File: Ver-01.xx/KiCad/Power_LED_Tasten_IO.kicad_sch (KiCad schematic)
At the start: 45 parts

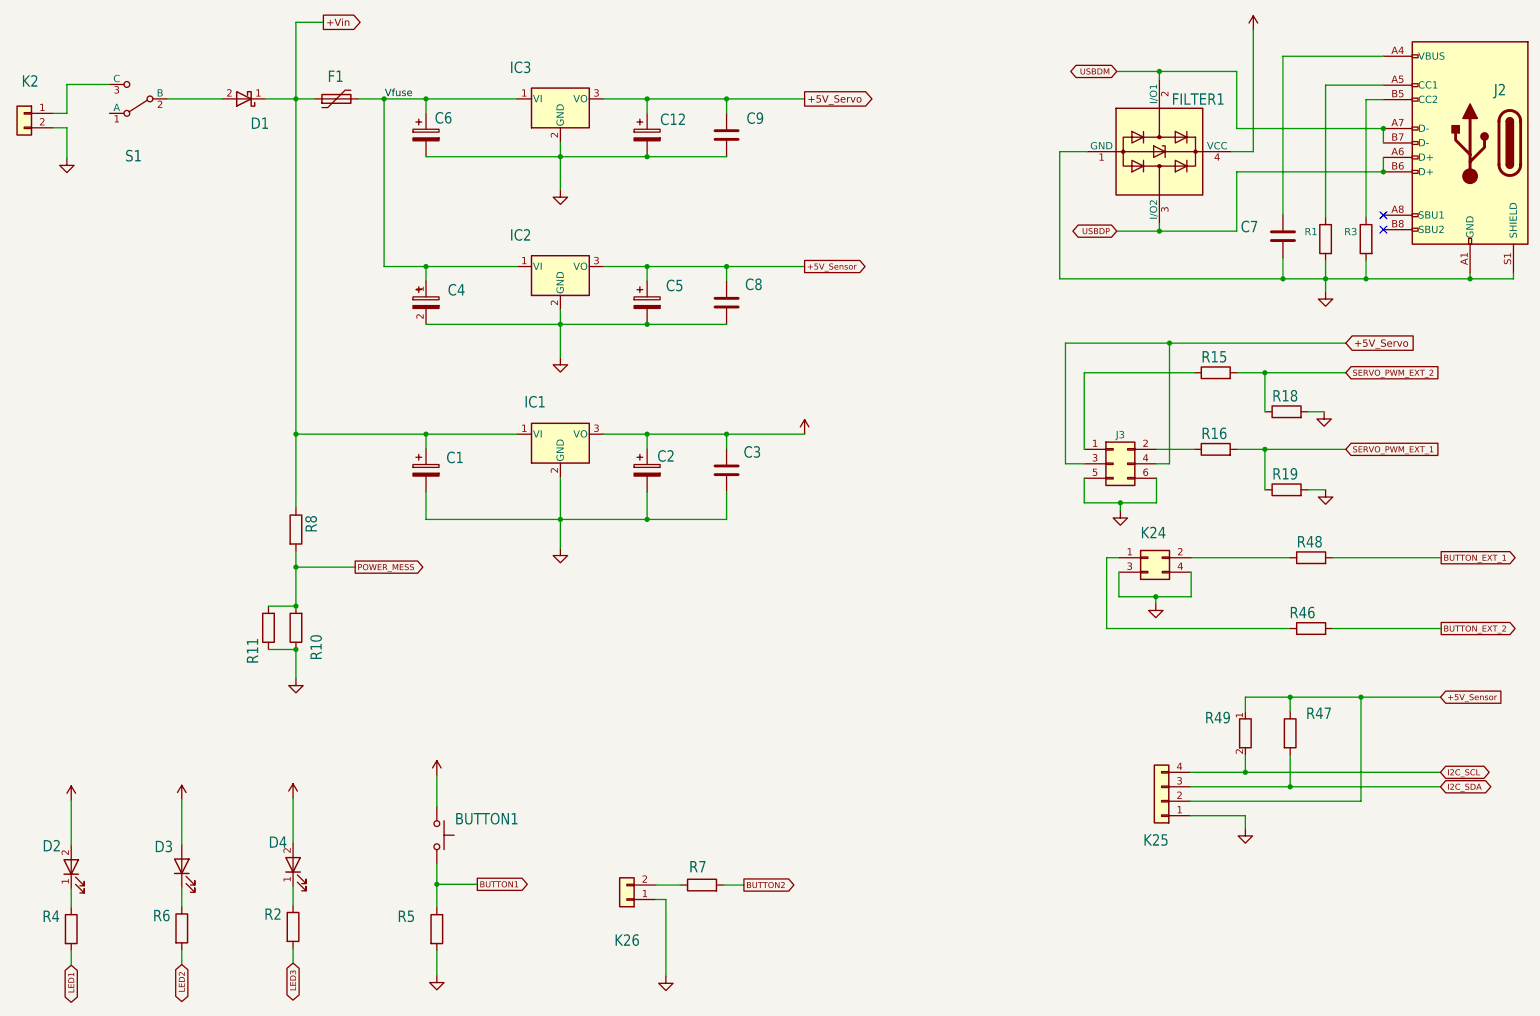
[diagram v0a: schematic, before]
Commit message: Snap to grid
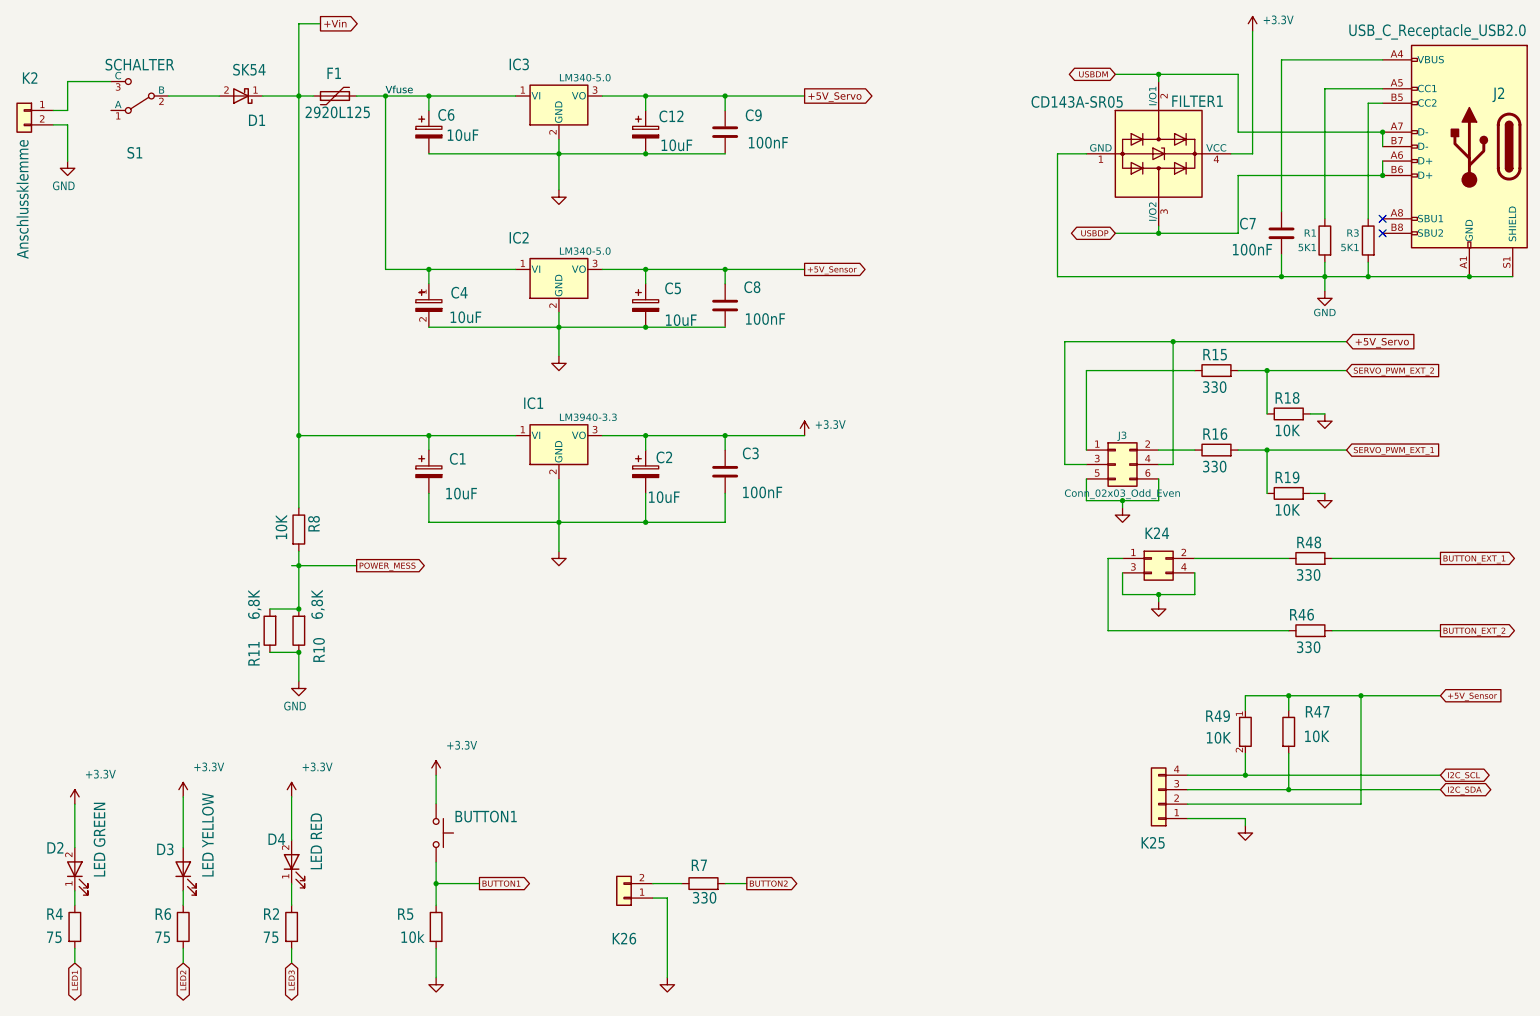
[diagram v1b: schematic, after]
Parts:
- BUTTON1: value (none) -> Taster_SMD; footprint (none) -> Button_Switch_SMD:SW_Push_1P1T_NO_6x6mm_H9.5mm
- C1, C12, C2, C4, C5, C6: value (none) -> 10uF; footprint (none) -> Capacitor_Tantalum_SMD:CP_EIA-3528-12_Kemet-T
- C3, C7, C8, C9: value (none) -> 100nF; footprint (none) -> Capacitor_SMD:C_0805_2012Metric
- D1: value (none) -> SK54; footprint (none) -> Diode_SMD:D_2512_6332Metric
- D2: value (none) -> LED GREEN; footprint (none) -> LED_SMD:LED_0805_2012Metric
- D3: value (none) -> LED YELLOW; footprint (none) -> LED_SMD:LED_0805_2012Metric
- D4: value (none) -> LED RED; footprint (none) -> LED_SMD:LED_0805_2012Metric
- F1: value (none) -> 2920L125; footprint (none) -> Fuse:Fuse_2920_7451Metric
- FILTER1: value (none) -> CD143A-SR05; footprint (none) -> Package_TO_SOT_SMD:SOT-143
- IC1: value (none) -> LM3940-3.3; footprint (none) -> Package_TO_SOT_SMD:SOT-223-3_TabPin2
- IC2, IC3: value (none) -> LM340-5.0; footprint (none) -> Package_TO_SOT_SMD:SOT-223-3_TabPin2
- J2: value (none) -> USB_C_Receptacle_USB2.0; footprint (none) -> Connector_USB:USB_C_Receptacle_JAE_DX07S016JA1R1500
- J3: value (none) -> Conn_02x03_Odd_Even; footprint (none) -> ORB:PinHeader_2x03_P2.54mm_Horizontal
- K2: value (none) -> Anschlussklemme; footprint (none) -> ORB:PinHeader_1x02_P2.54mm_Horizontal
- K24: value (none) -> Stiftleiste_2x02; footprint (none) -> ORB:PinHeader_2x02_P2.54mm_Horizontal
- K25: value (none) -> Stiftleiste_1x04; footprint (none) -> Connector_PinHeader_2.54mm:PinHeader_1x04_P2.54mm_Vertical
- K26: value (none) -> Stiftleiste_1x02_G_2,54; footprint (none) -> Connector_PinHeader_2.54mm:PinHeader_1x02_P2.54mm_Vertical
- R1, R3: value (none) -> 5K1; footprint (none) -> Resistor_SMD:R_0603_1608Metric
- R10, R11: value (none) -> 6,8K; footprint (none) -> Resistor_SMD:R_0603_1608Metric
- R15, R16, R46, R48, R7: value (none) -> 330; footprint (none) -> Resistor_SMD:R_0603_1608Metric
- R18, R19, R47, R49, R8: value (none) -> 10K; footprint (none) -> Resistor_SMD:R_0603_1608Metric
- R2, R4, R6: value (none) -> 75; footprint (none) -> Resistor_SMD:R_0603_1608Metric
- R5: value (none) -> 10k; footprint (none) -> Resistor_SMD:R_0603_1608Metric
- S1: value (none) -> SCHALTER; footprint (none) -> ORB:SW_500SSP1S1M7QEA
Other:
- moved on the sheet: C1, C12, C4, C5, C6, C7, C8, C9, D1, D2, D3, D4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

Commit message: Kleinere Optimierungen
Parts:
- R18, R19, R47, R49, R8: OrderNr YAG1290CT-ND -> YAG1290DKR-ND
- R5: value 10k -> 10K; MPN RC0603FR-10330RL -> RC0603FR-0710KP; OrderNr 13-RC0603FR-10330RLCT-ND -> YAG1290DKR-ND
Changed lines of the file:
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@@
       (effects (font (size 1.27 1.27)) hide)
     )
-    (property "OrderNr" "YAG1290CT-ND" (id 6) (at 238.76 86.36 0)
+    (property "OrderNr" "YAG1290DKR-ND" (id 6) (at 238.76 86.36 0)
       (effects (font (size 1.27 1.27)) hide)
     )
@@
       (effects (font (size 1.27 1.27)) hide)
     )
-    (property "OrderNr" "YAG1290CT-ND" (id 6) (at 238.76 100.33 0)
+    (property "OrderNr" "YAG1290DKR-ND" (id 6) (at 238.76 100.33 0)
       (effects (font (size 1.27 1.27)) hide)
     )
@@
       (effects (font (size 2 1.7)) (justify right bottom))
     )
-    (property "Value" "10k" (id 1) (at 86.868 179.578 0)
+    (property "Value" "10K" (id 1) (at 86.868 179.578 0)
       (effects (font (size 2 1.7)) (justify right bottom))
     )
@@
       (effects (font (size 1.27 1.27)) hide)
     )
-    (property "MPN" "RC0603FR-10330RL" (id 5) (at 88.9 176.53 0)
-      (effects (font (size 1.27 1.27)) hide)
-    )
-    (property "OrderNr" "13-RC0603FR-10330RLCT-ND" (id 6) (at 88.9 176.53 0)
+    (property "MPN" "RC0603FR-0710KP" (id 5) (at 88.9 176.53 0)
+      (effects (font (size 1.27 1.27)) hide)
+    )
+    (property "OrderNr" "YAG1290DKR-ND" (id 6) (at 88.9 176.53 0)
       (effects (font (size 1.27 1.27)) hide)
     )
@@
       (effects (font (size 1.27 1.27)) hide)
     )
-    (property "OrderNr" "YAG1290CT-ND" (id 6) (at 64.77 106.68 0)
+    (property "OrderNr" "YAG1290DKR-ND" (id 6) (at 64.77 106.68 0)
       (effects (font (size 1.27 1.27)) hide)
     )
@@
       (effects (font (size 1.27 1.27)) hide)
     )
-    (property "OrderNr" "YAG1290CT-ND" (id 6) (at 231.14 142.24 0)
+    (property "OrderNr" "YAG1290DKR-ND" (id 6) (at 231.14 142.24 0)
       (effects (font (size 1.27 1.27)) hide)
     )
@@
       (effects (font (size 1.27 1.27)) hide)
     )
-    (property "OrderNr" "YAG1290CT-ND" (id 6) (at 238.76 142.24 0)
-      (effects (font (size 1.27 1.27)) hide)
-    )
+    (property "OrderNr" "YAG1290DKR-ND" (id 6) (at 238.76 142.24 0)
+      (effects (font (size 1.27 1.27)) hide)
+    )

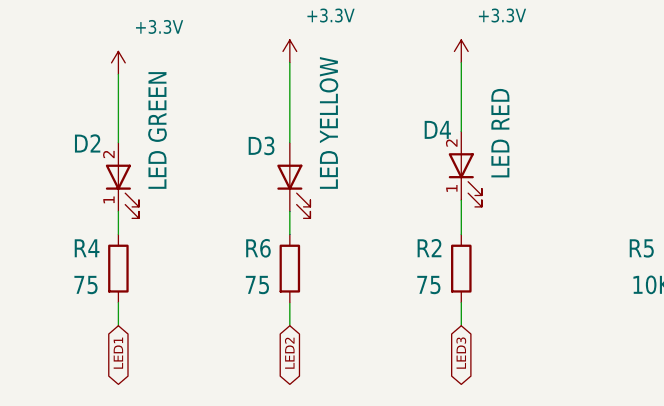
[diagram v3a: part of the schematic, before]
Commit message: After production test
Footprint D1 and Y1 changed.
LED shunt R=330
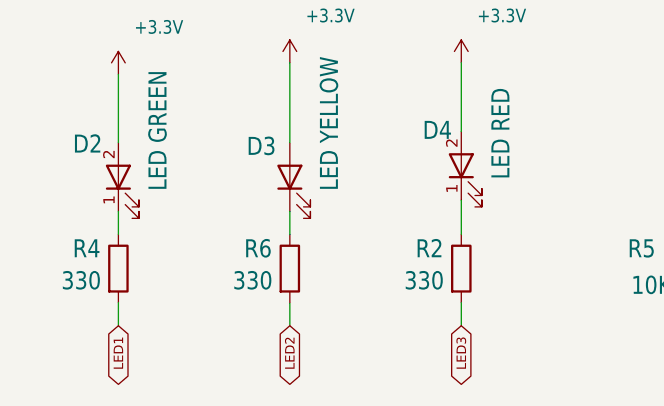
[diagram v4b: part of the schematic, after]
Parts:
- D1: footprint Diode_SMD:D_2512_6332Metric -> Diode_SMD:D_SMB
- R2, R4, R6: value 75 -> 330; MPN RC0603FR-0775RL -> RC0603FR-10330RL; OrderNr 311-75.0HRCT-ND -> 13-RC0603FR-10330RLCT-ND
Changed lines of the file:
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@@
       (effects (font (size 2 1.7)) (justify left bottom))
     )
-    (property "Value" "75" (at 58.42 179.578 0)
+    (property "Value" "330" (at 57.15 179.07 0)
       (effects (font (size 2 1.7)) (justify left bottom))
     )
@@
       (effects (font (size 1.27 1.27)) hide)
     )
-    (property "MPN" "RC0603FR-0775RL" (at 63.5 176.53 0)
-      (effects (font (size 1.27 1.27)) hide)
-    )
-    (property "OrderNr" "311-75.0HRCT-ND" (at 63.5 176.53 0)
+    (property "MPN" "RC0603FR-10330RL" (at 63.5 176.53 0)
+      (effects (font (size 1.27 1.27)) hide)
+    )
+    (property "OrderNr" "13-RC0603FR-10330RLCT-ND" (at 63.5 176.53 0)
       (effects (font (size 1.27 1.27)) hide)
     )
@@
       (effects (font (size 2 1.7)) (justify left bottom))
     )
-    (property "Value" "75" (at 39.37 179.578 0)
+    (property "Value" "330" (at 38.1 179.07 0)
       (effects (font (size 2 1.7)) (justify left bottom))
     )
@@
       (effects (font (size 1.27 1.27)) hide)
     )
-    (property "MPN" "RC0603FR-0775RL" (at 44.45 176.53 0)
-      (effects (font (size 1.27 1.27)) hide)
-    )
-    (property "OrderNr" "311-75.0HRCT-ND" (at 44.45 176.53 0)
+    (property "MPN" "RC0603FR-10330RL" (at 44.45 176.53 0)
+      (effects (font (size 1.27 1.27)) hide)
+    )
+    (property "OrderNr" "13-RC0603FR-10330RLCT-ND" (at 44.45 176.53 0)
       (effects (font (size 1.27 1.27)) hide)
     )
@@
       (effects (font (size 2 1.7)) (justify left bottom))
     )
-    (property "Value" "75" (at 20.32 179.578 0)
+    (property "Value" "330" (at 19.05 179.07 0)
       (effects (font (size 2 1.7)) (justify left bottom))
     )
@@
       (effects (font (size 1.27 1.27)) hide)
     )
-    (property "MPN" "RC0603FR-0775RL" (at 25.4 176.53 0)
-      (effects (font (size 1.27 1.27)) hide)
-    )
-    (property "OrderNr" "311-75.0HRCT-ND" (at 25.4 176.53 0)
+    (property "MPN" "RC0603FR-10330RL" (at 25.4 176.53 0)
+      (effects (font (size 1.27 1.27)) hide)
+    )
+    (property "OrderNr" "13-RC0603FR-10330RLCT-ND" (at 25.4 176.53 0)
       (effects (font (size 1.27 1.27)) hide)
     )
@@
       (effects (font (size 2 1.7)) (justify left bottom))
     )
-    (property "Footprint" "Diode_SMD:D_2512_6332Metric" (at 54.61 30.48 0)
-      (effects (font (size 1.27 1.27)) hide)
-    )
+    (property "Footprint" "Diode_SMD:D_SMB" (at 54.61 30.48 0)
+      (effects (font (size 1.27 1.27)) hide)
+    )

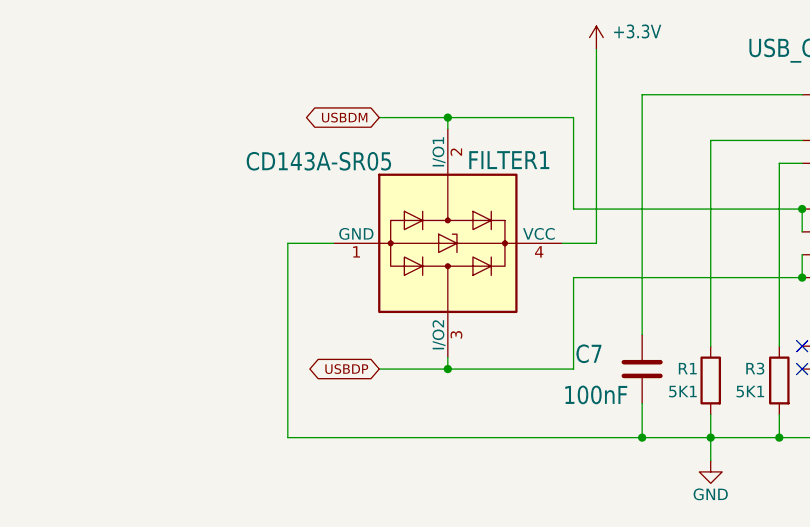
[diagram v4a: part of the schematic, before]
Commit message: USB connector changed
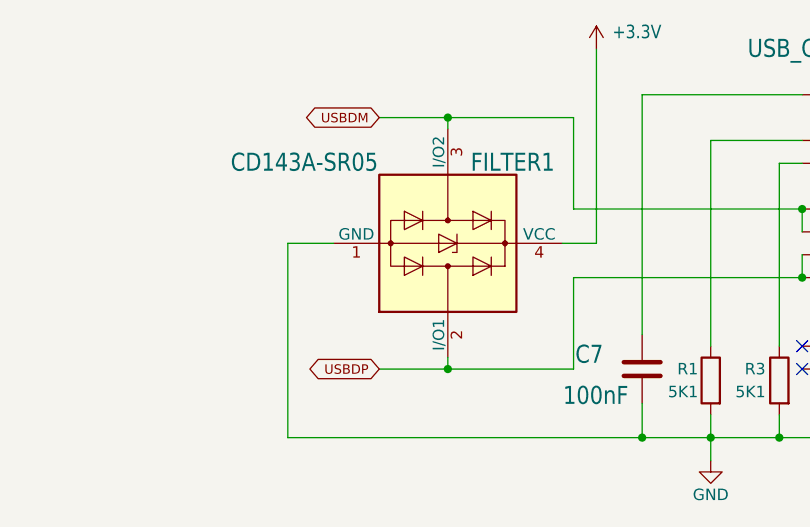
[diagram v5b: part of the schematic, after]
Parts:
- J2: footprint Connector_USB:USB_C_Receptacle_JAE_DX07S016JA1R1500 -> Connector_USB:USB_C_Receptacle_G-Switch_GT-USB-7010ASV; Distributor Digi-Key -> JLCPCB; MPN DX07S016JA1R1500 -> GT-USB-7010ASV; OrderNr 670-DX07S016JA1R1500TR-ND -> C2988369
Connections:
- net USBDM: now also FILTER1.3 (I/O2); no longer FILTER1.2 (I/O1)
- net USBDP: now also FILTER1.2 (I/O1); no longer FILTER1.3 (I/O2)
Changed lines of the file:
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@@
     )
   )
-  (symbol (lib_id "Power_Protection:PRTR5V0U2X") (at 215.9 40.64 270) (unit 1)
-    (in_bom yes) (on_board yes) (dnp no)
-    (property "Reference" "FILTER1" (at 218.059 32.639 90)
-      (effects (font (size 2 1.7)) (justify left bottom))
-    )
-    (property "Value" "CD143A-SR05" (at 193.421 32.766 90)
-      (effects (font (size 2 1.7)) (justify left bottom))
-    )
-    (property "Footprint" "Package_TO_SOT_SMD:SOT-143" (at 215.9 42.164 0)
-      (effects (font (size 1.27 1.27)) hide)
-    )
-    (property "Datasheet" "https://assets.nexperia.com/documents/data-sheet/PRTR5V0U2X.pdf" (at 215.9 42.164 0)
+  (symbol (lib_id "Power_Protection:PRTR5V0U2X") (at 215.9 40.64 270) (mirror x) (unit 1)
+    (in_bom yes) (on_board yes) (dnp no)
+    (property "Reference" "FILTER1" (at 218.44 30.48 90)
+      (effects (font (size 2 1.7)) (justify left bottom))
+    )
+    (property "Value" "CD143A-SR05" (at 191.77 30.48 90)
+      (effects (font (size 2 1.7)) (justify left bottom))
+    )
+    (property "Footprint" "Package_TO_SOT_SMD:SOT-143" (at 215.9 39.116 0)
+      (effects (font (size 1.27 1.27)) hide)
+    )
+    (property "Datasheet" "https://assets.nexperia.com/documents/data-sheet/PRTR5V0U2X.pdf" (at 215.9 39.116 0)
       (effects (font (size 1.27 1.27)) hide)
     )
@@
       (effects (font (size 2 1.7)) (justify left bottom))
     )
-    (property "Footprint" "Connector_USB:USB_C_Receptacle_JAE_DX07S016JA1R1500" (at 266.7 39.37 0)
-      (effects (font (size 1.27 1.27)) hide)
-    )
-    (property "Datasheet" "https://www.usb.org/sites/default/files/documents/usb_type-c.zip" (at 266.7 39.37 0)
-      (effects (font (size 1.27 1.27)) hide)
-    )
-    (property "MPN" "DX07S016JA1R1500" (at 270.51 39.37 0)
-      (effects (font (size 1.27 1.27)) hide)
-    )
-    (property "Distributor" "Digi-Key" (at 270.51 39.37 0)
-      (effects (font (size 1.27 1.27)) hide)
-    )
-    (property "OrderNr" "670-DX07S016JA1R1500TR-ND" (at 270.51 39.37 0)
-      (effects (font (size 1.27 1.27)) hide)
-    )
+    (property "Footprint" "Connector_USB:USB_C_Receptacle_G-Switch_GT-USB-7010ASV" (at 266.7 39.37 0)
+      (effects (font (size 1.27 1.27)) hide)
+    )
+    (property "Datasheet" "" (at 266.7 39.37 0)
+      (effects (font (size 1.27 1.27)) hide)
+    )
+    (property "MPN" "GT-USB-7010ASV" (at 270.51 39.37 0)
+      (effects (font (size 1.27 1.27)) hide)
+    )
+    (property "Distributor" "JLCPCB" (at 270.51 39.37 0)
+      (effects (font (size 1.27 1.27)) hide)
+    )
+    (property "OrderNr" "C2988369" (at 270.51 39.37 0)
+      (effects (font (size 1.27 1.27)) hide)
+    )
